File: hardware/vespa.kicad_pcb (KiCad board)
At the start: 2 copper layers, 256.5 x 100.3 mm, 119 parts, among them Q1 Q_PMOS, SW1 SW_Push, SW10 SW_Push, SW11 SW_Push, SW12 SW_Push, SW13 SW_Push, SW14 SW_Push, SW15 SW_Push, SW16 SW_Push, SW17 SW_Push, SW18 SW_Push, SW19 SW_Push, SW2 SW_Push, SW20 SW_Push, SW21 SW_Push, SW22 SW_Push, SW23 SW_Push, SW24 SW_Push, SW25 SW_Push, SW26 SW_Push, SW27 SW_Push, SW28 SW_Push, SW29 SW_Push, SW3 SW_Push, SW30 SW_Push, SW31 SW_Push, SW32 SW_Push, SW33 SW_Push, SW34 SW_Push, SW35 SW_Push, SW36 SW_Push, SW37 SW_Push, SW38 SW_Push, SW39 SW_Push, SW4 SW_Push, SW40 SW_Push, SW41 SW_Push, SW42 SW_Push, SW43 SW_Push, SW44 SW_Push, SW45 SW_Push, SW46 SW_Push, SW47 SW_Push, SW48 SW_Push, SW49 SW_Push, SW5 SW_Push, SW50 SW_Push, SW51 SW_Push, SW52 SW_Push, SW53 RotaryEncoder, SW54 SW_SPDT, SW6 SW_Push, SW7 SW_Push, SW8 SW_Push, SW9 SW_Push, U1 XIAO nRF52840 Plus, U2 XCL103D333CR-G, U3 BU4210G-TR

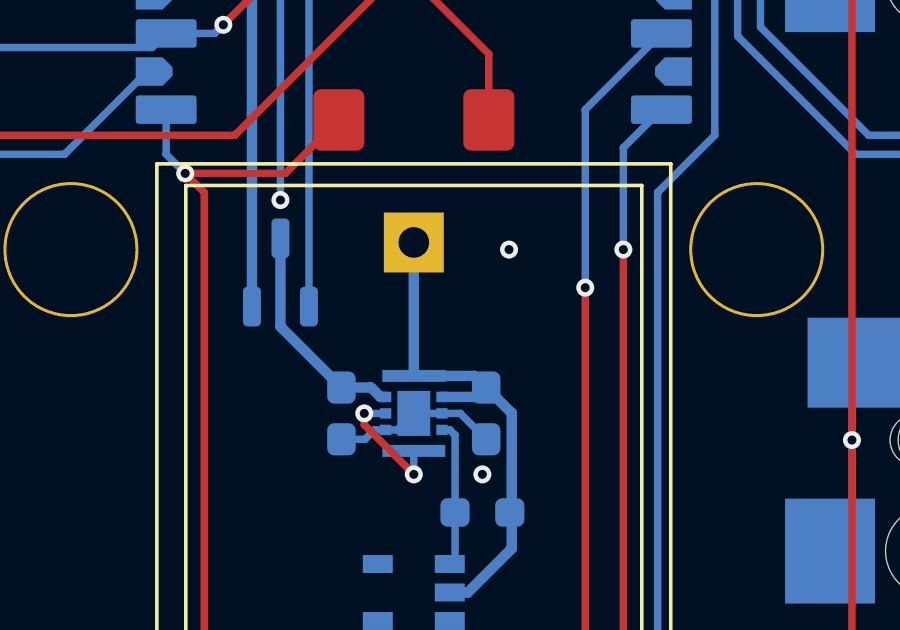
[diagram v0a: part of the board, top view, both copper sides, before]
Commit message: update dc-dc input routing
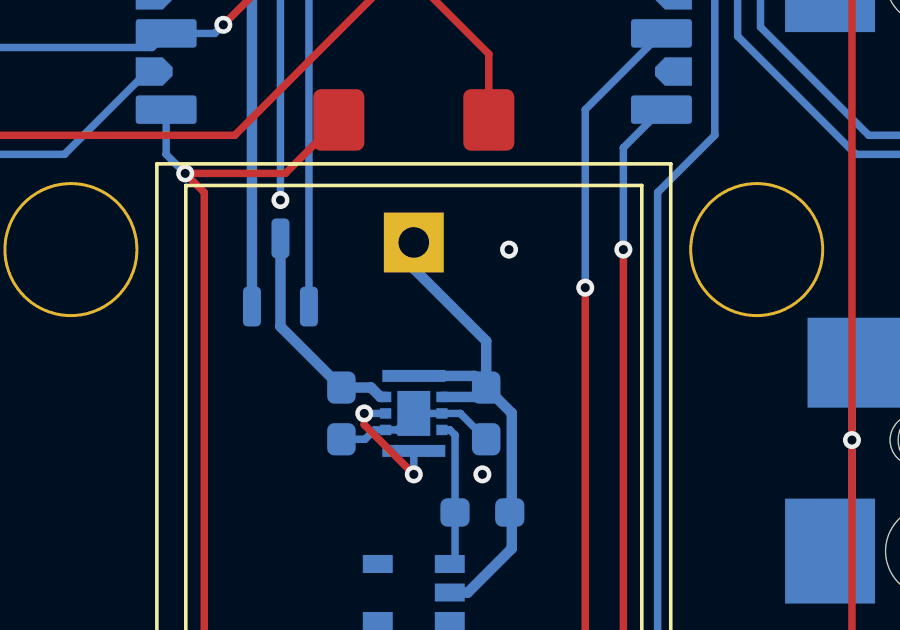
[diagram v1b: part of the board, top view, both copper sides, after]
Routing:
- net +BATT: track 17.0 -> 18.4 mm
